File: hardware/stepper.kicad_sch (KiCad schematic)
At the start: 2 parts, among them J1 Conn_01x04, U2 TMC2209-LA

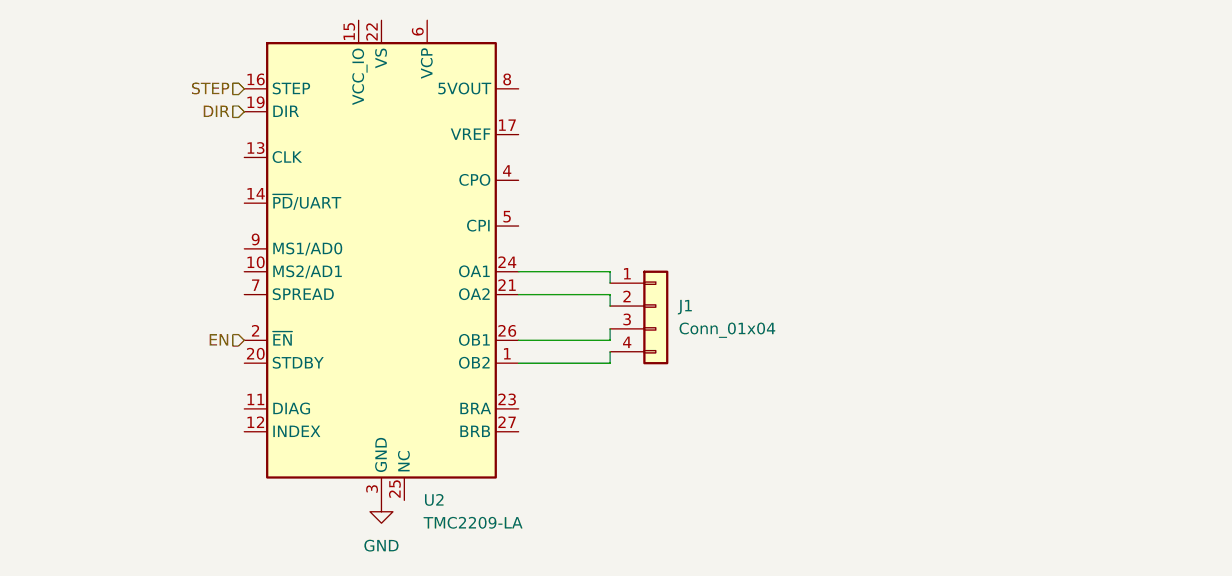
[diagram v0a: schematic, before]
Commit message: Explain why driver VIO must be 3.3 V, not 5 V
VIO sets the logic reference, not the operating supply, so 3.3 V costs
nothing. At 5 V the input threshold rises to ~3.5 V, above what the ESP32 can
drive, and - the damaging half - PDN_UART is bidirectional, so the driver
answers register reads at VIO and pushes 5 V into a GPIO that is not 5 V
tolerant. Both UART pins fan out to five drivers.
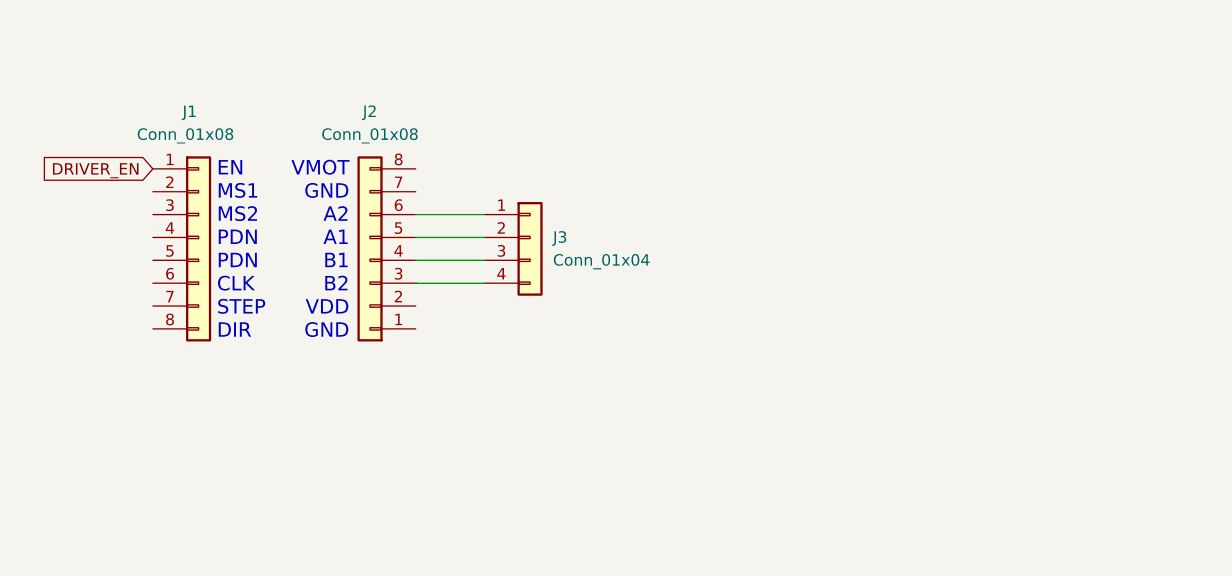
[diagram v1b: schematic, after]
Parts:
- removed J1: Conn_01x04, symbol Connector_Generic:Conn_01x04
- removed U2: TMC2209-LA, Package_DFN_QFN:VQFN-28-1EP_5x5mm_P0.5mm_EP3.7x3.7mm_ThermalVias, symbol Driver_Motor:TMC2209-LA
- added J1, J2: Conn_01x08, symbol Connector_Generic:Conn_01x08
- added J3: Conn_01x04, symbol Connector_Generic:Conn_01x04
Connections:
- new net: J2.6 (Pin_6), J3.1 (Pin_1)
- new net: J2.5 (Pin_5), J3.2 (Pin_2)
- new net: J2.4 (Pin_4), J3.3 (Pin_3)
- new net: J2.3 (Pin_3), J3.4 (Pin_4)
- new net DRIVER_EN: J1.1 (Pin_1)
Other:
- note added: "EN MS1 MS2 PDN PDN CLK STEP DIR"
- note added: "VMOT GND A2 A1 B1 B2 VDD GND"

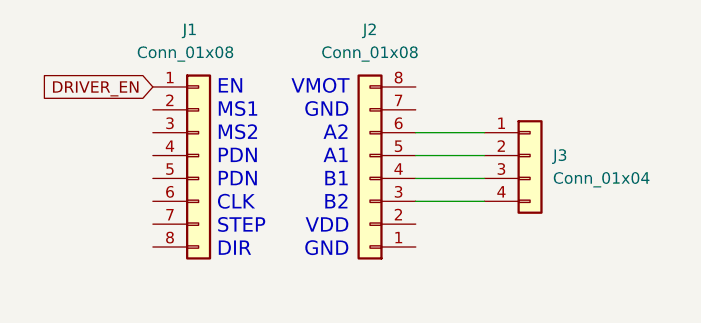
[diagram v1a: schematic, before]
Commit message: Resolve the two-PDN-pad question for BigTreeTech modules
BTT TMC2209 V1.2/V1.3 breaks PDN_UART out on two alternative pin positions,
not as TX and RX. Pin 4 is the factory default with the 1k already fitted on
the module; pin 5 is physically open until that resistor is relocated.

So: wire pin 4 to the bus, leave pin 5 NC, and add no external resistor - a
second 1k in series would make 2k. Klipper drives these from a single uart_pin,
confirming single-wire half-duplex, so the pin budget is unchanged and both the
SPI display header and the R8 option survive.

Notes that this is vendor-specific: bare ICs and Watterott SilentStepSticks do
not carry the resistor, and some modules genuinely split TX/RX.

Source: https://global.bttwiki.com/TMC2209.html
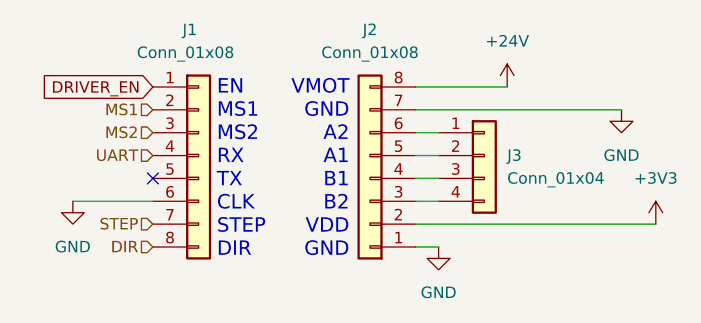
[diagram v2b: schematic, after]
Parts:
- J1, J2: footprint (none) -> Connector_PinSocket_2.54mm:PinSocket_1x08_P2.54mm_Vertical
- J3: footprint (none) -> Connector_PinHeader_2.54mm:PinHeader_1x04_P2.54mm_Vertical
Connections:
- net MS1: now reaches J1.2 (Pin_2)
- net MS2: now reaches J1.3 (Pin_3)
- net UART: now reaches J1.4 (Pin_4)
- net GND: now reaches J1.6 (Pin_6)
- net GND: now also J2.1 (Pin_1), J2.7 (Pin_7)
- net STEP: now reaches J1.7 (Pin_7)
- net DIR: now reaches J1.8 (Pin_8)
- net +3V3: now reaches J2.2 (Pin_2)
- net +24V: now reaches J2.8 (Pin_8)
- no-connect marks 0 -> 1
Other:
- note added: "EN MS1 MS2 RX TX CLK STEP DIR"
- note removed: "EN MS1 MS2 PDN PDN CLK STEP DIR"
- moved on the sheet: J3

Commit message: make the schematics
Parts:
- added C10: 100 uF, electrolytic, symbol Device:C
- added C15: 100 nF, symbol Device:C
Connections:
- net +24V: now also C10.1, C15.1
- net GND: now also C10.2, C15.2

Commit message: place the stuff on the pcb
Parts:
- removed C15: 100 nF, symbol Device:C
- C10: value 100 uF, electrolytic -> 100 uF, 50V electrolytic; footprint (none) -> Capacitor_THT:C_Radial_D8.0mm_H11.5mm_P3.50mm; JLC Part# (none) -> C2749; MFR Part# (none) -> KM107M050F12RR0VH2FP0
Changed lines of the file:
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@@
-	)
-	(junction
-		(at 165.1 71.12)
-		(diameter 0)
-		(color 0 0 0 0)
-	)
-	(junction
-		(at 181.61 78.74)
-		(diameter 0)
-		(color 0 0 0 0)
 	)
 	(junction
@@
 	(wire
 		(pts
-			(xy 165.1 71.12) (xy 181.61 71.12)
-		)
-		(stroke
-			(width 0)
-			(type default)
-		)
-	)
-	(wire
-		(pts
 			(xy 128.27 81.28) (xy 125.73 81.28)
 		)
@@
 	(wire
 		(pts
-			(xy 125.73 71.12) (xy 165.1 71.12)
-		)
-		(stroke
-			(width 0)
-			(type default)
-		)
-	)
-	(wire
-		(pts
 			(xy 152.4 86.36) (xy 125.73 86.36)
 		)
@@
 	(wire
 		(pts
-			(xy 181.61 78.74) (xy 165.1 78.74)
+			(xy 125.73 71.12) (xy 181.61 71.12)
 		)
 		(stroke
@@
 			)
 			(justify right)
-		)
-	)
-	(symbol
-		(lib_id "Device:C")
-		(at 165.1 74.93 0)
-		(unit 1)
-		(body_style 1)
-		(exclude_from_sim no)
-		(in_bom yes)
-		(on_board yes)
-		(in_pos_files yes)
-		(dnp no)
-		(fields_autoplaced yes)
-		(property "Reference" "C15"
-			(at 168.91 73.6599 0)
-			(show_name no)
-			(do_not_autoplace no)
-			(effects
-				(font
-					(size 1.27 1.27)
-				)
-				(justify left)
-			)
-		)
-		(property "Value" "100 nF"
-			(at 168.91 76.1999 0)
-			(show_name no)
-			(do_not_autoplace no)
-			(effects
-				(font
-					(size 1.27 1.27)
-				)
-				(justify left)
-			)
-		)
-		(property "Footprint" ""
-			(at 166.0652 78.74 0)
-			(hide yes)
-			(show_name no)
-			(do_not_autoplace no)
-			(effects
-				(font
-					(size 1.27 1.27)
-				)
-			)
-		)
-		(property "Datasheet" ""
-			(at 165.1 74.93 0)
-			(hide yes)
-			(show_name no)
-			(do_not_autoplace no)
-			(effects
-				(font
-					(size 1.27 1.27)
-				)
-			)
-		)
-		(property "Description" "Unpolarized capacitor"
-			(at 165.1 74.93 0)
-			(hide yes)
-			(show_name no)
-			(do_not_autoplace no)
-			(effects
-				(font
-					(size 1.27 1.27)
-				)
-			)
-		)
-		(pin "1"
-		)
-		(pin "2"
-		)
-		(instances
-			(project "ufluidics"
-				(path "/bf8ba2d7-3b7b-4865-bab6-5f38b618ecb0/0490ac22-4186-4de0-867f-92f23bb002cb"
-					(reference "C17")
-					(unit 1)
-				)
-				(path "/bf8ba2d7-3b7b-4865-bab6-5f38b618ecb0/3dcc8c7c-7b82-4ea2-a1ed-aae4ec1cfffa"
-					(reference "C19")
-					(unit 1)
-				)
-				(path "/bf8ba2d7-3b7b-4865-bab6-5f38b618ecb0/864cedd2-718f-4cca-b038-6c3e6245f1a2"
-					(reference "C18")
-					(unit 1)
-				)
-				(path "/bf8ba2d7-3b7b-4865-bab6-5f38b618ecb0/c869babf-cbcf-4a53-91eb-8705d939d0f5"
-					(reference "C15")
-					(unit 1)
-				)
-				(path "/bf8ba2d7-3b7b-4865-bab6-5f38b618ecb0/e1c4a126-6ec3-4200-a557-ebfb82816ed4"
-					(reference "C16")
-					(unit 1)
-				)
-			)
 		)
 	)
@@
 			)
 		)
-		(property "Value" "100 uF, electrolytic"
+		(property "Value" "100 uF, 50V electrolytic"
 			(at 185.42 76.1999 0)
 			(show_name no)
@@
 			)
 		)
-		(property "Footprint" ""
+		(property "Footprint" "Capacitor_THT:C_Radial_D8.0mm_H11.5mm_P3.50mm"
 			(at 182.5752 78.74 0)
 			(hide yes)
@@
 			)
 		)
-		(property "Description" "Unpolarized capacitor"
+		(property "Description" "100uF 12mm 2000hrs@105℃ 3.5mm 50V 8mm ±20% 插件,D8xL12mm Aluminum Electrolytic Capacitors - Leaded ROHS"
 			(at 181.61 74.93 0)
 			(hide yes)
+			(show_name no)
+			(do_not_autoplace no)
+			(effects
+				(font
+					(size 1.27 1.27)
+				)
+			)
+		)
+		(property "MFR Part#" "KM107M050F12RR0VH2FP0"
+			(at 181.61 74.93 0)
+			(hide yes)
+			(show_name no)
+			(do_not_autoplace no)
+			(effects
+				(font
+					(size 1.27 1.27)
+				)
+			)
+		)
+		(property "JLC Part#" "C2749"
+			(at 181.61 74.93 0)
+			(hide yes)
